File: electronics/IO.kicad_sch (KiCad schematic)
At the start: 17 parts, among them SW1 RotaryEncoder_Switch, SW2 RotaryEncoder_Switch

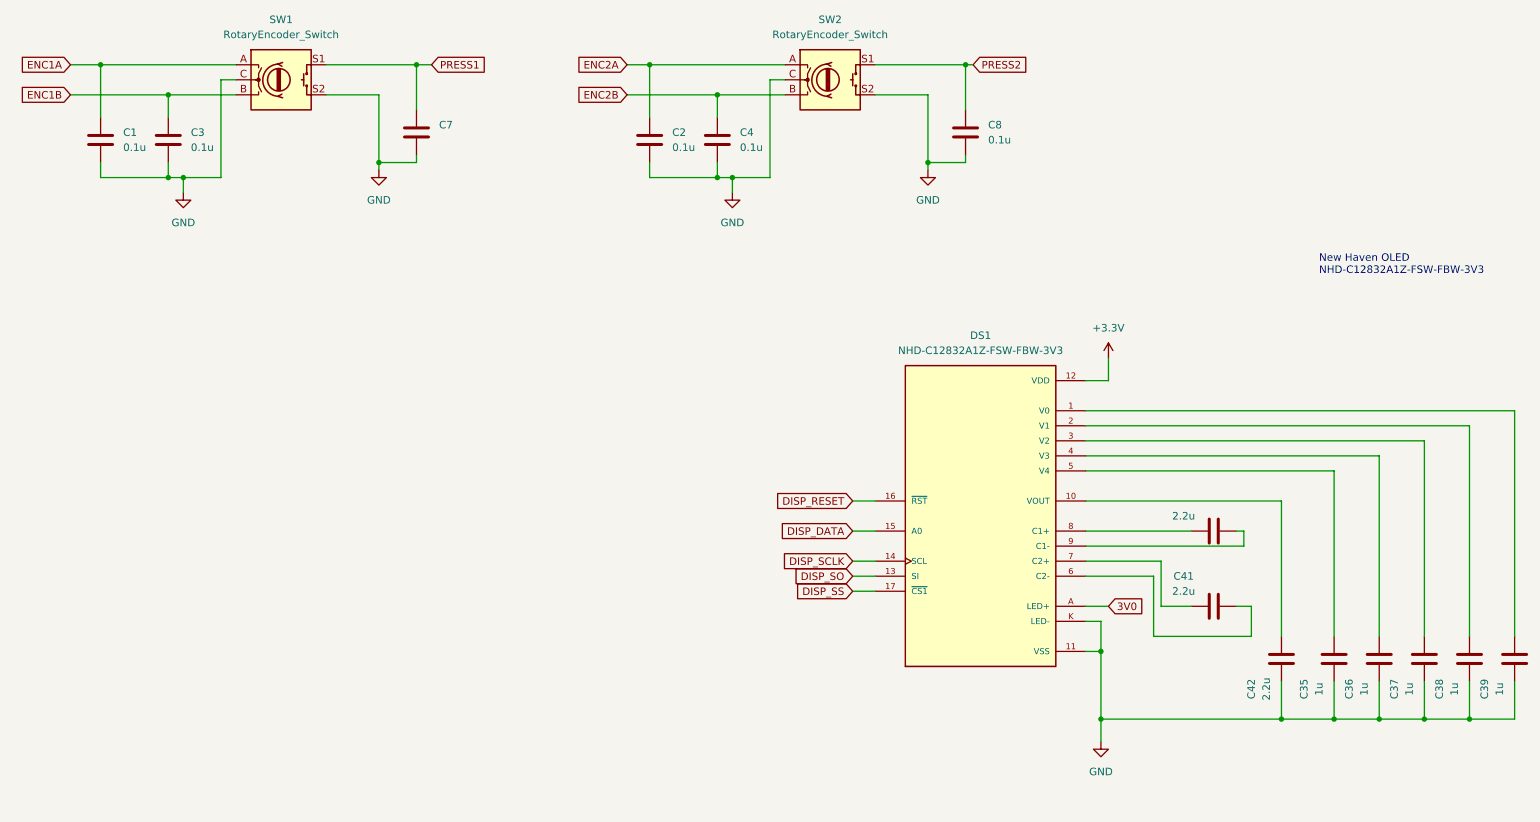
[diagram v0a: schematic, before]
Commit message: Many changes to the design. Fully routed.
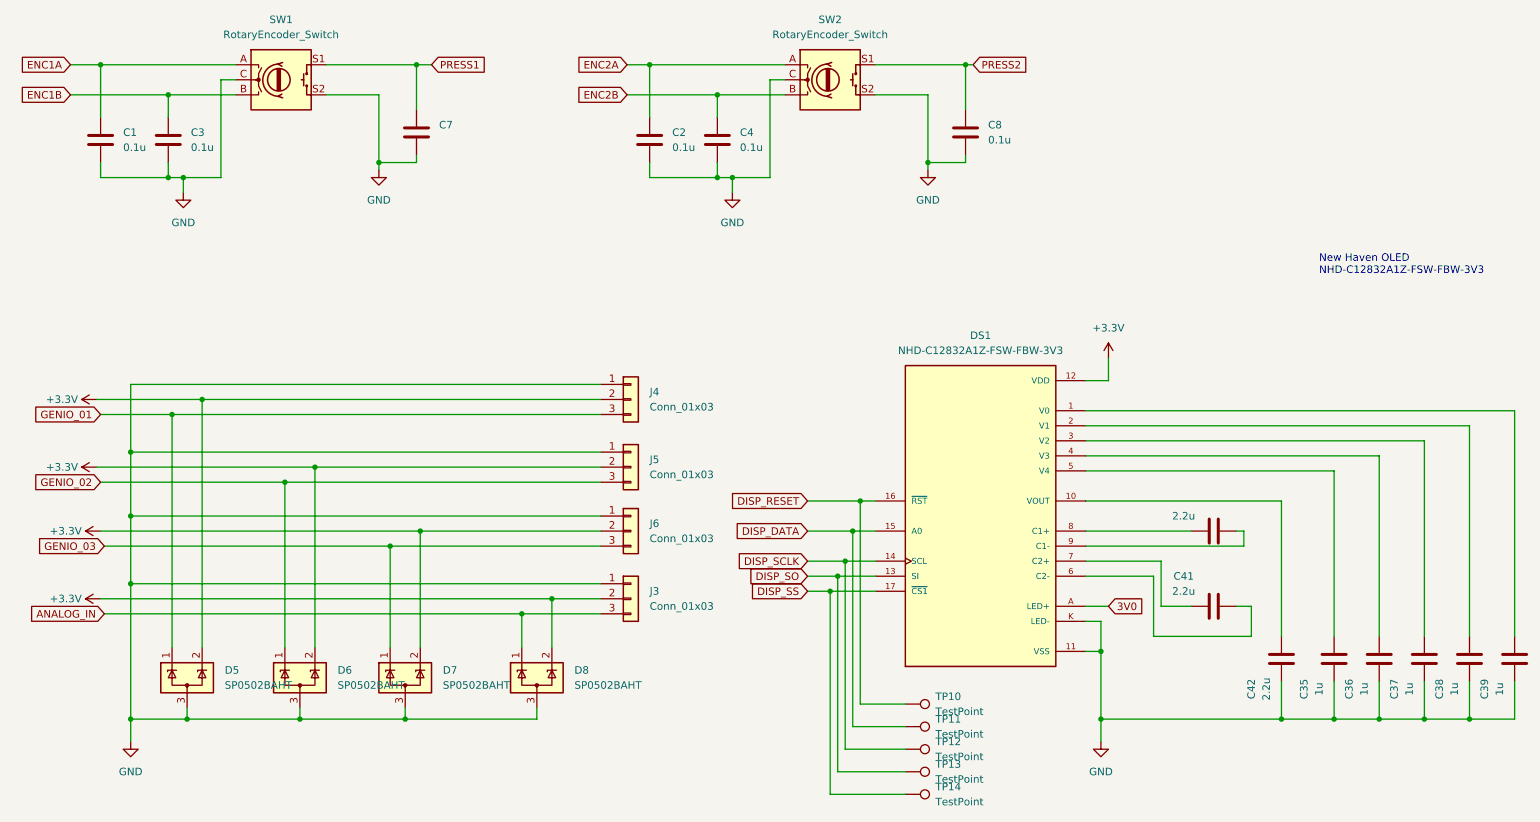
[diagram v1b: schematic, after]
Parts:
- added D5, D6, D7, D8: SP0502BAHT, Package_TO_SOT_SMD:SOT-23, symbol Power_Protection:SP0502BAHT
- added J3, J4, J5, J6: Conn_01x03, Connector_PinSocket_2.54mm:PinSocket_1x03_P2.54mm_Vertical, symbol Connector_Generic:Conn_01x03
- added TP10, TP11, TP12, TP13, TP14: TestPoint, TestPoint:TestPoint_Pad_D1.0mm, symbol Connector:TestPoint
- C1, C2, C3, C35, C36, C37, C38, C39, C4, C40, C41, C42, C7, C8: footprint Capacitor_SMD:C_0603_1608Metric_Pad1.08x0.95mm_HandSolder -> Capacitor_SMD:C_0402_1005Metric
- SW1, SW2: JLCPCB (none) -> 987-1195-ND
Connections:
- net +3.3V: now also D5.2 (K), D6.2 (K), D7.2 (K), D8.2 (K), J3.2 (Pin_2), J4.2 (Pin_2), J5.2 (Pin_2), J6.2 (Pin_2)
- net DISP_DATA: now also TP11.1
- net DISP_RESET: now also TP10.1
- net DISP_SCLK: now also TP12.1
- net DISP_SO: now also TP13.1
- net DISP_SS: now also TP14.1
- net GND: now also D5.3 (A), D6.3 (A), D7.3 (A), D8.3 (A), J3.1 (Pin_1), J4.1 (Pin_1), J5.1 (Pin_1), J6.1 (Pin_1)
- new net ANALOG_IN: D8.1 (K), J3.3 (Pin_3)
- new net GENIO_01: D5.1 (K), J4.3 (Pin_3)
- new net GENIO_02: D6.1 (K), J5.3 (Pin_3)
- new net GENIO_03: D7.1 (K), J6.3 (Pin_3)

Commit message: Almost sent this to fab. It is getting expensive.
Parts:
- C1, C2, C3, C4, C7, C8: JLCPCB (none) -> C2655418
- D5, D6, D7, D8: JLCPCB (none) -> C207261
- DS1, J3, J4, J5, J6, TP10, TP11, TP12, TP13, TP14: now not fitted
- SW1, SW2: Digikey (none) -> 987-1195-ND; JLCPCB 987-1195-ND -> (none); now not fitted

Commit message: Ordered this version.
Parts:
- C1, C2, C3, C4, C7, C8: JLCPCB C2655418 -> C432917
- C40, C41, C42: footprint Capacitor_SMD:C_0402_1005Metric -> Capacitor_SMD:C_0603_1608Metric; JLCPCB (none) -> C76612
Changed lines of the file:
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@@
 			)
 		)
-		(property "JLCPCB" "C2655418 "
+		(property "JLCPCB" "C432917"
 			(at 41.91 40.64 0)
 			(effects
@@
 			)
 		)
-		(property "Footprint" "Capacitor_SMD:C_0402_1005Metric"
+		(property "Footprint" "Capacitor_SMD:C_0603_1608Metric"
 			(at 222.25 105.7148 0)
 			(effects
@@
 		)
 		(property "Description" ""
+			(at 218.44 106.68 0)
+			(effects
+				(font
+					(size 1.27 1.27)
+				)
+				(hide yes)
+			)
+		)
+		(property "JLCPCB" "C76612"
 			(at 218.44 106.68 0)
 			(effects
@@
 			)
 		)
-		(property "JLCPCB" "C2655418 "
+		(property "JLCPCB" "C432917"
 			(at 176.53 39.37 0)
 			(effects
@@
 			)
 		)
-		(property "JLCPCB" "C2655418 "
+		(property "JLCPCB" "C432917"
 			(at 30.48 40.64 0)
 			(effects
@@
 			)
 		)
-		(property "JLCPCB" "C2655418 "
+		(property "JLCPCB" "C432917"
 			(at 134.62 40.64 0)
 			(effects
@@
 			)
 		)
-		(property "Footprint" "Capacitor_SMD:C_0402_1005Metric"
+		(property "Footprint" "Capacitor_SMD:C_0603_1608Metric"
 			(at 222.25 118.4148 0)
 			(effects
@@
 		)
 		(property "Description" ""
+			(at 218.44 119.38 0)
+			(effects
+				(font
+					(size 1.27 1.27)
+				)
+				(hide yes)
+			)
+		)
+		(property "JLCPCB" "C76612"
 			(at 218.44 119.38 0)
 			(effects
@@
 			)
 		)
-		(property "JLCPCB" "C2655418 "
+		(property "JLCPCB" "C432917"
 			(at 83.82 39.37 0)
 			(effects
@@
 			)
 		)
-		(property "JLCPCB" "C2655418 "
+		(property "JLCPCB" "C432917"
 			(at 123.19 40.64 0)
 			(effects
@@
 			)
 		)
-		(property "Footprint" "Capacitor_SMD:C_0402_1005Metric"
+		(property "Footprint" "Capacitor_SMD:C_0603_1608Metric"
 			(at 228.9048 124.46 0)
 			(effects
@@
 			(at 229.87 128.27 0)
 			(effects
+				(font
+					(size 1.27 1.27)
+				)
+				(hide yes)
+			)
+		)
+		(property "JLCPCB" "C76612"
+			(at 229.87 128.27 0)
+			(effects

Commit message: Tweaked parts to use Basic parts which are cheaper.
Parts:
- C1, C2, C3, C4, C7, C8: JLCPCB C432917 -> C1525
- C40, C41, C42: JLCPCB C76612 -> C23630
- D5, D6, D7, D8: JLCPCB C207261 -> C32677
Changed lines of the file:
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@@
 			)
 		)
-		(property "JLCPCB" "C432917"
+		(property "JLCPCB" "C1525"
 			(at 41.91 40.64 0)
 			(effects
@@
 			)
 		)
-		(property "JLCPCB" "C76612"
+		(property "JLCPCB" "C23630"
 			(at 218.44 106.68 0)
 			(effects
@@
 			)
 		)
-		(property "JLCPCB" "C207261"
+		(property "JLCPCB" "C32677"
 			(at 64.135 131.445 0)
 			(effects
@@
 			)
 		)
-		(property "JLCPCB" "C432917"
+		(property "JLCPCB" "C1525"
 			(at 176.53 39.37 0)
 			(effects
@@
 			)
 		)
-		(property "JLCPCB" "C432917"
+		(property "JLCPCB" "C1525"
 			(at 30.48 40.64 0)
 			(effects
@@
 			)
 		)
-		(property "JLCPCB" "C207261"
+		(property "JLCPCB" "C32677"
 			(at 45.085 131.445 0)
 			(effects
@@
 			)
 		)
-		(property "JLCPCB" "C432917"
+		(property "JLCPCB" "C1525"
 			(at 134.62 40.64 0)
 			(effects
@@
 			)
 		)
-		(property "JLCPCB" "C76612"
+		(property "JLCPCB" "C23630"
 			(at 218.44 119.38 0)
 			(effects
@@
 			)
 		)
-		(property "JLCPCB" "C207261"
+		(property "JLCPCB" "C32677"
 			(at 81.915 131.445 0)
 			(effects
@@
 			)
 		)
-		(property "JLCPCB" "C432917"
+		(property "JLCPCB" "C1525"
 			(at 83.82 39.37 0)
 			(effects
@@
 			)
 		)
-		(property "JLCPCB" "C432917"
+		(property "JLCPCB" "C1525"
 			(at 123.19 40.64 0)
 			(effects
@@
 			)
 		)
-		(property "JLCPCB" "C76612"
+		(property "JLCPCB" "C23630"
 			(at 229.87 128.27 0)
 			(effects
@@
 			)
 		)
-		(property "JLCPCB" "C207261"
+		(property "JLCPCB" "C32677"
 			(at 104.14 131.445 0)
 			(effects

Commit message: Ordered this version.
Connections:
- net DISP_SO renamed DISP_SI
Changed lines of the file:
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@@
 		)
 	)
-	(global_label "DISP_SO"
+	(global_label "DISP_SI"
 		(shape input)
 		(at 149.86 114.3 180)
@@
 		)
 		(property "Intersheetrefs" "${INTERSHEET_REFS}"
-			(at 139.0129 114.3 0)
+			(at 139.7386 114.3 0)
 			(effects
 				(font

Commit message: Made some changes and thought I should check it in.
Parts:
- DS1: now fitted
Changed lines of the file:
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@@
 		(in_bom yes)
 		(on_board yes)
-		(dnp yes)
+		(dnp no)
 		(fields_autoplaced yes)
 		(property "Reference" "DS1"

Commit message: Updated design for REV B.
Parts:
- removed D7, D8: SP0502BAHT, Package_TO_SOT_SMD:SOT-23, symbol Power_Protection:SP0502BAHT
- removed J3, J4, J5, J6: Conn_01x03, Connector_PinSocket_2.54mm:PinSocket_1x03_P2.54mm_Vertical, symbol Connector_Generic:Conn_01x03
- added J3: Conn_01x06, Connector_JST:JST_PH_S6B-PH-K_1x06_P2.00mm_Horizontal, symbol Connector_Generic:Conn_01x06
- C1, C2, C3, C4: value 0.1u -> 10n; JLCPCB C1525 -> C57112
- SW1, SW2: Digikey 987-1195-ND -> PEC11R-4220K-S0024-ND
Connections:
- net +3.3V: now also J3.1 (Pin_1); no longer D5.2 (K), D6.2 (K)
- net ANALOG_IN: now also D6.2 (K), J3.6 (Pin_6)
- net GENIO_01: now also J3.3 (Pin_3)
- net GENIO_02: now also D5.2 (K), J3.4 (Pin_4); no longer D6.1 (K)
- net GENIO_03: now also D6.1 (K), J3.5 (Pin_5)
- net GND: now also J3.2 (Pin_2)
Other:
- moved on the sheet: D5, D6

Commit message: This version is working well. Need to figure out USB DFU programming.
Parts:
- C1, C2, C3, C4: JLCPCB C57112 -> C15195
- C35, C36, C37, C38, C39: JLCPCB (none) -> C52923
- J3: Digikey (none) -> 455-1723-ND
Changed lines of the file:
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@@
 			)
 		)
-		(property "JLCPCB" "C57112"
+		(property "JLCPCB" "C15195"
 			(at 41.91 40.64 0)
 			(effects
@@
 			)
 		)
+		(property "Digikey" "455-1723-ND"
+			(at 91.44 86.36 0)
+			(effects
+				(font
+					(size 1.27 1.27)
+				)
+				(hide yes)
+			)
+		)
 		(pin "4"
 		)
@@
 			)
 		)
+		(property "JLCPCB" "C52923"
+			(at 254 128.27 0)
+			(effects
+				(font
+					(size 1.27 1.27)
+				)
+				(hide yes)
+			)
+		)
 		(pin "2"
 		)
@@
 			)
 		)
-		(property "JLCPCB" "C57112"
+		(property "JLCPCB" "C15195"
 			(at 30.48 40.64 0)
 			(effects
@@
 			)
 		)
-		(property "JLCPCB" "C57112"
+		(property "JLCPCB" "C15195"
 			(at 134.62 40.64 0)
 			(effects
@@
 			)
 		)
+		(property "JLCPCB" "C52923"
+			(at 238.76 128.27 0)
+			(effects
+				(font
+					(size 1.27 1.27)
+				)
+				(hide yes)
+			)
+		)
 		(pin "2"
 		)
@@
 			)
 		)
-		(property "JLCPCB" "C57112"
+		(property "JLCPCB" "C15195"
 			(at 123.19 40.64 0)
 			(effects
@@
 			)
 		)
+		(property "JLCPCB" "C52923"
+			(at 261.62 128.27 0)
+			(effects
+				(font
+					(size 1.27 1.27)
+				)
+				(hide yes)
+			)
+		)
 		(pin "2"
 		)
@@
 		)
 		(property "Description" ""
+			(at 246.38 128.27 0)
+			(effects
+				(font
+					(size 1.27 1.27)
+				)
+				(hide yes)
+			)
+		)
+		(property "JLCPCB" "C52923"
 			(at 246.38 128.27 0)
 			(effects
@@
 			(at 269.24 128.27 0)
 			(effects
+				(font
+					(size 1.27 1.27)
+				)
+				(hide yes)
+			)
+		)
+		(property "JLCPCB" "C52923"
+			(at 269.24 128.27 0)
+			(effects
